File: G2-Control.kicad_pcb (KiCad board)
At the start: 2 copper layers, 100 x 100 mm, 90 parts, among them J1 Conn_01x06_Pin, J102 Conn_01x06_Pin, J103 Conn_01x06_Pin, J104 Board Interconnect, J2 Q2_link, J3 Conn_01x07_Pin, J4 Conn_01x05_Pin, K1 SMI-12VDC-SL-2C, K2 SMI-12VDC-SL-2C, K3 SMI-12VDC-SL-2C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

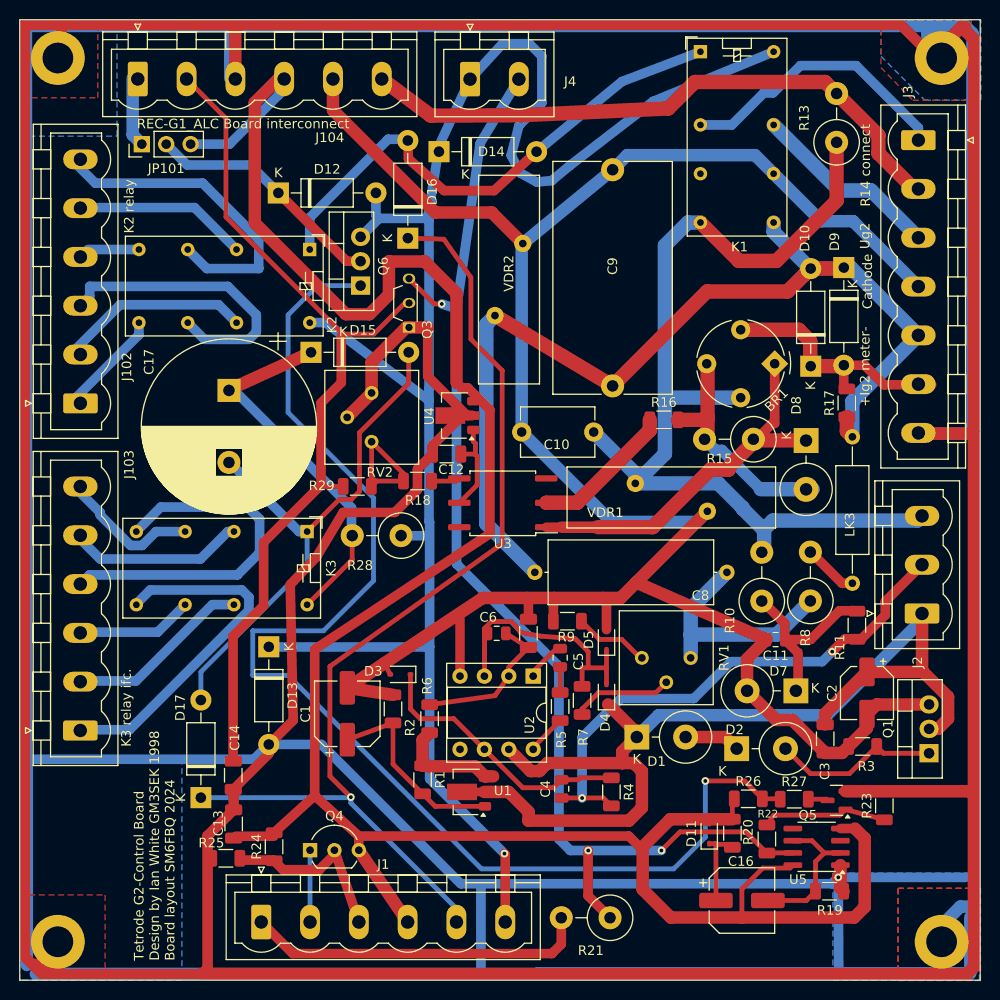
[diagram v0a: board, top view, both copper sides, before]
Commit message: Fixes for issues #7 #6 #3 #5
Connected U1 correctly.
Added D6 to the board
Added version number to silkscreen text.
Added high voltage warning
Turned Q1 around and moved it closer to the edge.
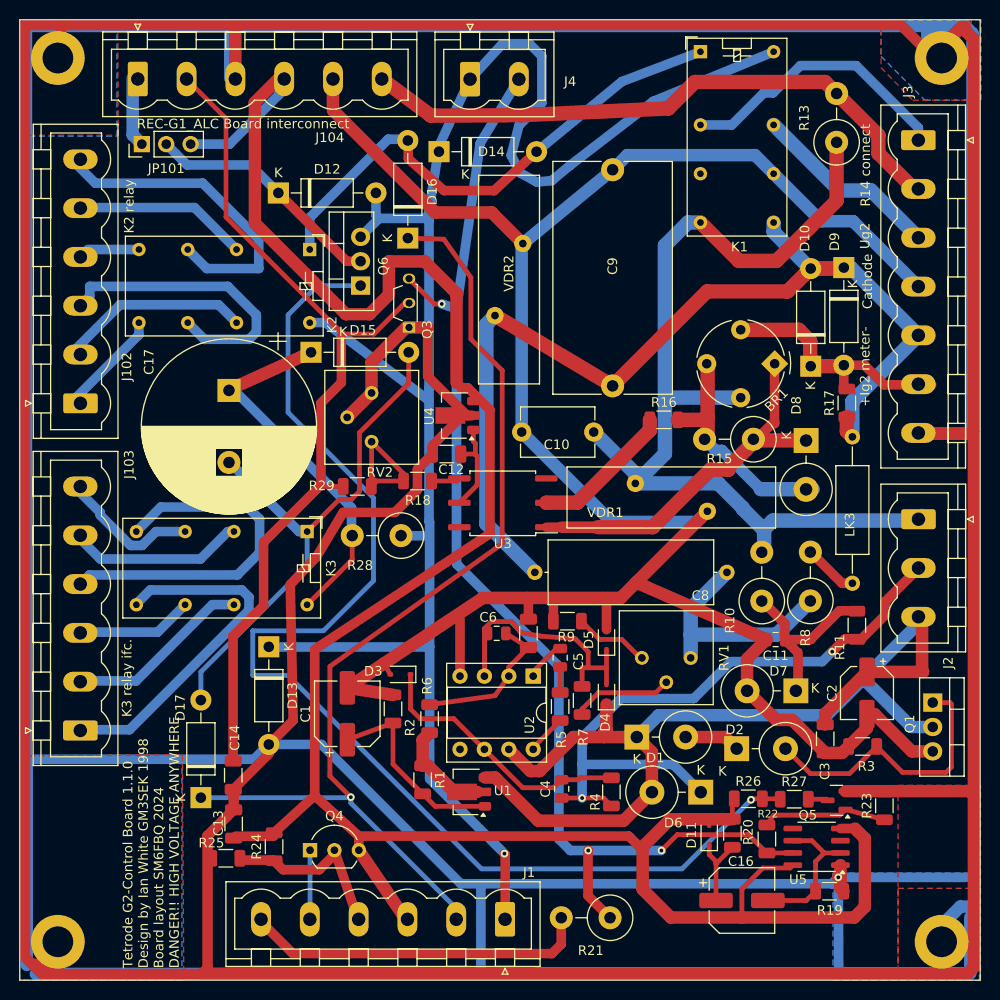
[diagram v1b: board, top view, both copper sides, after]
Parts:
- added D6: BZX55C12V, Diode_THT:D_DO-201_P5.08mm_Vertical_KathodeUp, F.Cu at (150.9, 120.4)
- moved J1 25.4 mm to (130.6, 133.7), turned to 180 degrees
- moved J2 9.82 mm to (173.6, 92.0), turned to -90 degrees
- moved Q1 5.29 mm to (175.1, 111.1), turned to -90 degrees
- moved D11 0.16 mm to (151.8, 124.9)
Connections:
- J1 pad 1: ALARM_LED_CATHODE -> +12/24V HV ENABLE
- J1 pad 2: ALARM_LED_ANODE -> PTT_L
- J1 pad 3: RESET-A -> +12V REG IN
- J1 pad 4: +12V REG IN -> RESET-A
- J1 pad 5: PTT_L -> ALARM_LED_ANODE
- J1 pad 6: +12/24V HV ENABLE -> ALARM_LED_CATHODE
- J2 pad 1: /+30V rail -> /R12
- J2 pad 3: /R12 -> /+30V rail
- R1 pad 1: Net-(U1-VI) -> Net-(U1-VO)
- R6 pad 1: Net-(U1-VI) -> Net-(U1-VO)
- U1 pad 2: /+30V rail -> Net-(U1-VO)
- U1 pad 3: Net-(U1-VI) -> /+30V rail
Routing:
- net /Q2G: track 55.5 -> 69.0 mm
- net Net-(D2-A): track 17.5 -> 29.4 mm
- net Net-(U1-VI): track 11.5 -> 0.00 mm
- net Net-(U1-VO): track 0.00 -> 10.6 mm
- net Net-(Q6-G): track 130.7 -> 125.8 mm
- net CATHODE: track 232.0 -> 233.6 mm
- net /+30V rail: track 108.7 -> 110.1 mm
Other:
- board text added: "Tetrode G2-Control Board 1.1.0 Design by Ian White GM3SEK 1998 Board layout SM6FBQ 2024 DANGER!! HIGH VOLTAGE ANYWHERE"
- board text removed: "Tetrode G2-Control Board Design by Ian White GM3SEK 1998 Board layout SM6FBQ 2024"

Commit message: Added a mounting hole below VDR2 and copper zones around to get a good grounding point for CATHODE when using the board for cathode grounded PA's. This is suggested in G3SEK's writeup "Power and Protection for Modern Tetrodes" on page 9. This is a guard against "Ground bounces" in case of flashover in the tubes.
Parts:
- added H5: MountingHole_Pad, MountingHole:MountingHole_3.2mm_M3_DIN965_Pad, F.Cu at (128.3, 63.5)
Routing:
- net CATHODE: track 233.6 -> 240.3 mm
- net PTT_L: track 107.4 -> 105.6 mm
- net Aux trip in: track 124.3 -> 125.9 mm
- net +12/24V HV ENABLE: track 190.6 -> 191.7 mm
- net Net-(D14-A): track 55.2 -> 54.3 mm
- net +12V REG IN: track 241.4 -> 240.8 mm
- added copper zone on B.Cu, net CATHODE
- added copper zone on F.Cu, net CATHODE
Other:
- board text added: "Tetrode G2-Control Board 2.0.0 Design by Ian White GM3SEK 1998 Board layout SM6FBQ 2024 DANGER!! HIGH VOLTAGE"
- board text removed: "Tetrode G2-Control Board 1.1.0 Design by Ian White GM3SEK 1998 Board layout SM6FBQ 2024 DANGER!! HIGH VOLTAGE ANYWHERE"
